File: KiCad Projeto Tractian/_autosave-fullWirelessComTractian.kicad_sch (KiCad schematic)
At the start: 28 parts, among them U1 ESP8266EX, U2 MX25R3235FM2xx1, U4 MX25R3235FM2xx1, U5 AMS1117-3.3, U6 TMP36xS, Y2 XTAL 16Mhz ±10ppm (TSX -3225 )

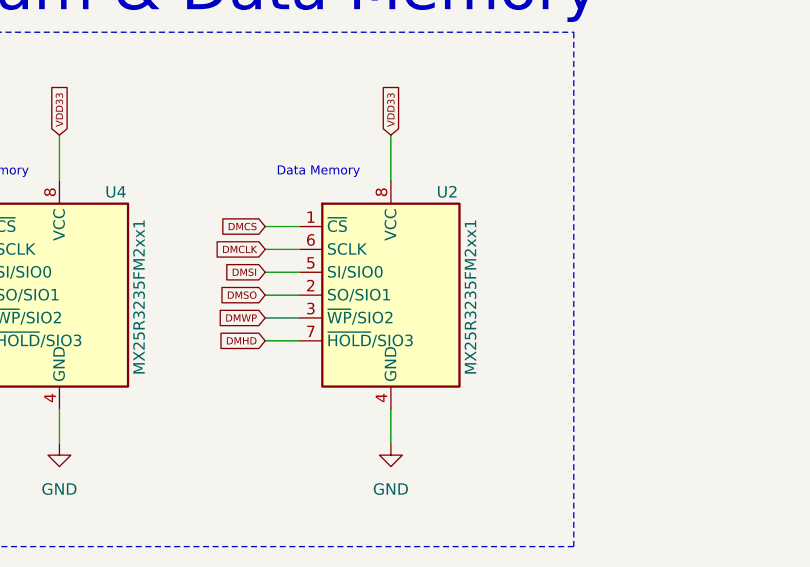
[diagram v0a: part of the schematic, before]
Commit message: :bug: fix da Read subroutine
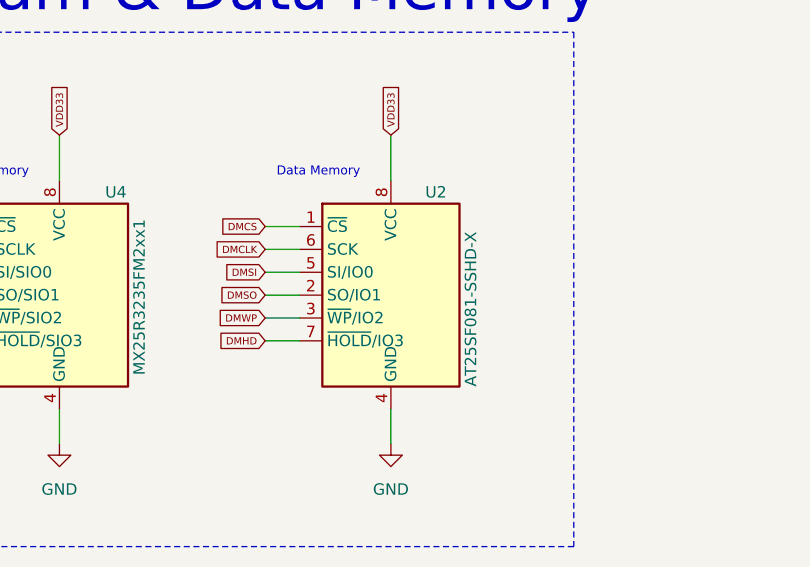
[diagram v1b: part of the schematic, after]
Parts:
- removed U2: MX25R3235FM2xx1, Package_SO:SOP-8_5.28x5.23mm_P1.27mm, symbol Memory_Flash:MX25R3235FM2xx1
- added U2: AT25SF081-SSHD-X, Package_SO:SOIC-8_3.9x4.9mm_P1.27mm, symbol Memory_Flash:AT25SF081-SSHD-X
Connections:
- net DMCLK: now also U2.6 (SCK)
- net DMCS: now also U2.1 (~{CS})
- net DMHD: now also U2.7 (~{HOLD}/IO3)
- net DMSI: now also U2.5 (SI/IO0)
- net DMSO: now also U2.2 (SO/IO1)
- net DMWP: now also U2.3 (~{WP}/IO2)
- net GND: now also U2.4 (GND)
- net VDD33: now also U2.8 (VCC)
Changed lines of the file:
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@@
+    )
+  )
+  (symbol (lib_id "Memory_Flash:AT25SF081-SSHD-X") (at 251.46 52.07 0) (unit 1)
+    (in_bom yes) (on_board yes) (dnp no)
+    (property "Reference" "U2" (at 255.27 40.64 0)
+      (effects (font (size 1.27 1.27)) (justify left))
+    )
+    (property "Value" "AT25SF081-SSHD-X" (at 260.35 62.23 90)
+      (effects (font (size 1.27 1.27)) (justify left))
+    )
+    (property "Footprint" "Package_SO:SOIC-8_3.9x4.9mm_P1.27mm" (at 251.46 67.31 0)
+      (effects (font (size 1.27 1.27)) hide)
+    )
+    (property "Datasheet" "https://www.adestotech.com/wp-content/uploads/DS-AT25SF081_045.pdf" (at 251.46 52.07 0)
+      (effects (font (size 1.27 1.27)) hide)
+    )
+    (pin "1")
+    (pin "2")
+    (pin "3")
+    (pin "4")
+    (pin "5")
+    (pin "6")
+    (pin "7")
+    (pin "8")
+    (instances
+      (project "fullWirelessComTractian"
+        (path "/de37416f-2273-481a-bd7e-d92c2e99b78a"
+          (reference "U2") (unit 1)
+        )
+      )
     )
   )
@@
         )
       )
-    )
-  )
-  (symbol (lib_id "Memory_Flash:MX25R3235FM2xx1") (at 251.46 52.07 0) (unit 1)
-    (in_bom yes) (on_board yes) (dnp no)
-    (property "Reference" "U2" (at 256.54 40.64 0)
-      (effects (font (size 1.27 1.27)) (justify left))
-    )
-    (property "Value" "MX25R3235FM2xx1" (at 260.35 60.96 90)
-      (effects (font (size 1.27 1.27)) (justify left))
-    )
-    (property "Footprint" "Package_SO:SOP-8_5.28x5.23mm_P1.27mm" (at 251.46 67.31 0)
-      (effects (font (size 1.27 1.27)) hide)
-    )
-    (property "Datasheet" "http://www.macronix.com/Lists/Datasheet/Attachments/7534/MX25R3235F,%20Wide%20Range,%2032Mb,%20v1.6.pdf" (at 251.46 52.07 0)
-      (effects (font (size 1.27 1.27)) hide)
-    )
-    (pin "1")
-    (pin "2")
-    (pin "3")
-    (pin "4")
-    (pin "5")
-    (pin "6")
-    (pin "7")
-    (pin "8")
-    (instances
-      (project "fullWirelessComTractian"
-        (path "/de37416f-2273-481a-bd7e-d92c2e99b78a"
-          (reference "U2") (unit 1)
-        )
-      )

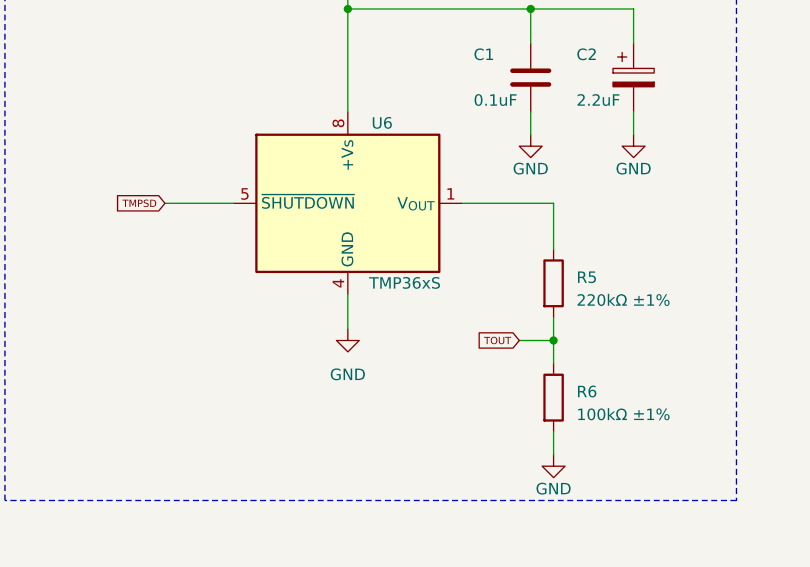
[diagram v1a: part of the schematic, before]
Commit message: :rocket: Rotina de leitura de temperatura com estabilizacao por filtro LTI media movel
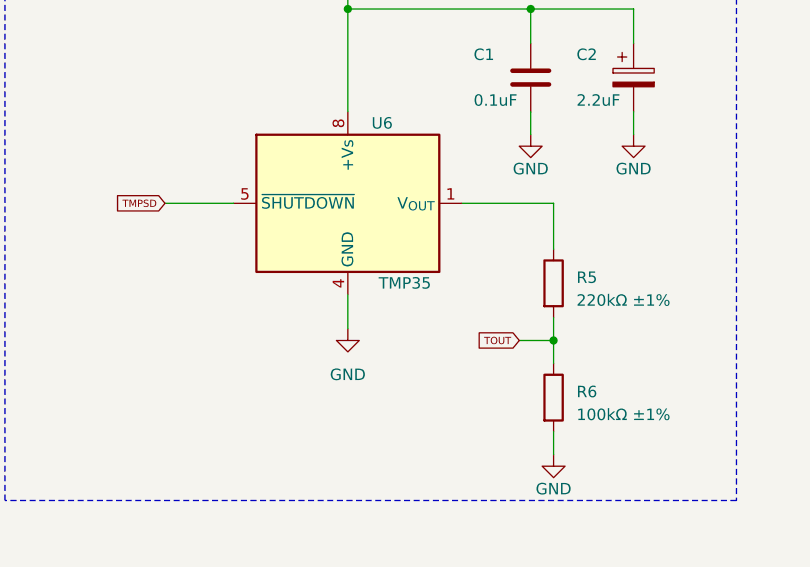
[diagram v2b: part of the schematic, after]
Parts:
- U6: value TMP36xS -> TMP35
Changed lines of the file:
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@@
       (effects (font (size 1.27 1.27)))
     )
-    (property "Value" "TMP36xS" (at 236.22 139.7 0)
+    (property "Value" "TMP35" (at 236.22 139.7 0)
       (effects (font (size 1.27 1.27)))
     )
